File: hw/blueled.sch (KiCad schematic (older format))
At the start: 54 parts, among them J1 Barrel_Jack, J2 LED Strip, J3 ICSP, J4 Screw_Terminal_01x02, Q1 Q_PMOS_SDG, Q2 Q_PNP_EBC, SW2 PUSH, U1 ATmega328P-AU, U2 HC-05, U3 AMS1117-3.3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

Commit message: add(hw): resistor for ENA of DC/DC
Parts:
- added R12: 1k, Resistor_SMD:R_0805_2012Metric_Pad1.15x1.40mm_HandSolder, symbol Device:R
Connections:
- wire segments 197 -> 198
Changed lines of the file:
@@
 U 1 1 5FB2573B
 P 2200 1250
-F 0 "D4" H 2350 1350 50  0000 L CNN
-F 1 "D_Zener_ALT" H 2000 1450 50  0000 L CNN
+F 0 "D4" V 2200 1300 50  0000 L CNN
+F 1 "D_Zener_ALT" H 2000 1450 50  0001 L CNN
 F 2 "Diode_SMD:D_SOD-123" H 2200 1250 50  0001 C CNN
 F 3 "https://datasheet.lcsc.com/szlcsc/1912111437_PANJIT-International-MMSZ5240B_C268602.pdf" H 2200 1250 50  0001 C CNN
@@
 Wire Wire Line
 	2200 1000 2200 750
-Text Label 2800 2400 2    50   ~ 0
+Text Label 2800 2000 2    50   ~ 0
 PWR_PRT
 $Comp
@@
 Text Notes 750  5900 0    50   ~ 0
 Transistor is used to \nreset HC-05\nIt's need to switch to \nAT mode
+$Comp
+L Device:R R12
+U 1 1 5FD06E35
+P 2800 2250
+F 0 "R12" H 2870 2296 50  0000 L CNN
+F 1 "1k" H 2870 2205 50  0000 L CNN
+F 2 "Resistor_SMD:R_0805_2012Metric_Pad1.15x1.40mm_HandSolder" V 2730 2250 50  0001 C CNN
+F 3 "https://datasheet.lcsc.com/szlcsc/1810301711_KOA-Speer-Elec-RK73B2ATTD102J_C159911.pdf" H 2800 2250 50  0001 C CNN
+F 4 "lcsc.com" H 2800 2250 50  0001 C CNN "Distributor"
+F 5 "RK73B2ATTD102J" H 2800 2250 50  0001 C CNN "Manuf. Part"
+	1    2800 2250
+	1    0    0    -1
+$EndComp
+Wire Wire Line
+	2800 2000 2800 2100
 $EndSCHEMATC

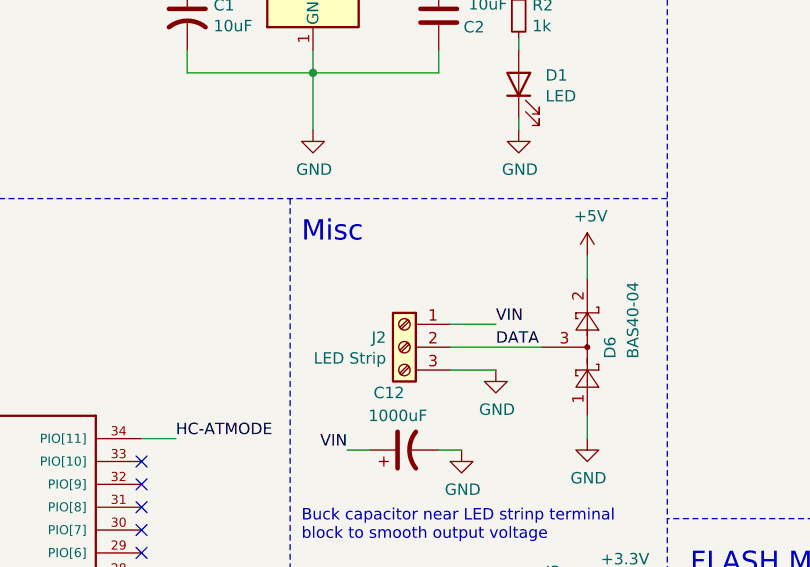
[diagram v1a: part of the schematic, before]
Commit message: add: better terminal block for led connection
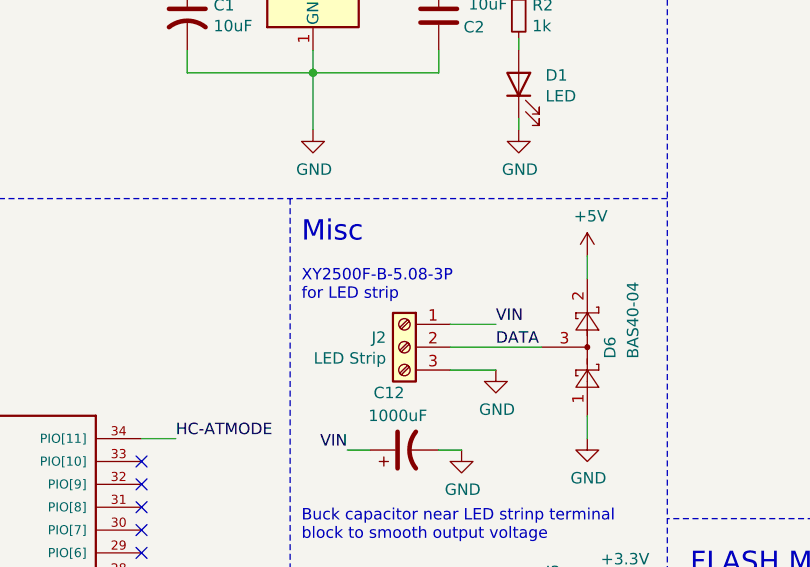
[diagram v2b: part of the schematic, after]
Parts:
- J2: footprint TerminalBlock:TerminalBlock_bornier-3_P5.08mm -> (none); Manuf. Part 1729131 -> XY2500R-D-5.08-3P
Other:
- note added: "XY2500F-B-5.08-3P \nfor LED strip\n"
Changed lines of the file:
@@
 F 0 "J2" H 5880 3842 50  0000 L CNN
 F 1 "LED Strip" H 5880 3751 50  0000 L CNN
-F 2 "TerminalBlock:TerminalBlock_bornier-3_P5.08mm" H 5800 3800 50  0001 C CNN
-F 3 "https://datasheet.lcsc.com/szlcsc/1811151432_Phoenix-Contact-1729131_C91154.pdf" H 5800 3800 50  0001 C CNN
+F 2 "" H 5800 3800 50  0001 C CNN
+F 3 "https://datasheet.lcsc.com/szlcsc/2004291906_Ningbo-Xinlaiya-Elec-XY2500R-D-5-08-3P_C505825.pdf" H 5800 3800 50  0001 C CNN
 F 4 "lcsc.com" H 5800 3800 50  0001 C CNN "Distributor"
-F 5 "1729131" H 5800 3800 50  0001 C CNN "Manuf. Part"
+F 5 "XY2500R-D-5.08-3P" H 5800 3800 50  0001 C CNN "Manuf. Part"
 	1    5800 3800
 	-1   0    0    -1
@@
 Wire Wire Line
 	2800 2000 2800 2100
+Text Notes 5350 3600 0    50   ~ 0
+XY2500F-B-5.08-3P \nfor LED strip\n
 $EndSCHEMATC

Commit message: fix: EN should be floating
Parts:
- removed R12: 1k, Resistor_SMD:R_0805_2012Metric_Pad1.15x1.40mm_HandSolder, symbol Device:R
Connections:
- wire segments 198 -> 195
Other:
- note added: "Float it to Enable"
- moved on the sheet: S1
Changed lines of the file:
@@
 Wire Wire Line
 	8850 3750 8950 3750
-Wire Wire Line
-	2900 2400 2800 2400
-NoConn ~ 2900 2900
-NoConn ~ 3300 2800
+NoConn ~ 2900 2650
+NoConn ~ 3300 2550
 $Comp
 L power:GND #PWR0110
@@
 	1    0    0    -1
 $EndComp
-NoConn ~ 2900 2700
+NoConn ~ 2900 2450
 $Comp
 L blueled-rescue:SWITCH-DPDT-PTH-GPI-152-3013-SparkFun-Switches S1
 U 1 1 5EB8E526
-P 3100 2700
-F 0 "S1" H 3100 2250 45  0000 C CNN
-F 1 "SWITCH-DPDT-PTH-GPI-152-3013" H 3100 3176 45  0001 C CNN
-F 2 "blueled:XKB7070-Z" H 3100 3150 20  0001 C CNN
-F 3 "https://datasheet.lcsc.com/szlcsc/2002271810_XKB-Enterprise-XKB7070-Z_C318863.pdf" H 3100 2700 50  0001 C CNN
-F 4 "SWCH-10554" H 3100 3081 60  0001 C CNN "Field4"
-F 5 "lcsc.com" H 3100 2700 50  0001 C CNN "Distributor"
-F 6 "XKB7070-Z" H 3100 2700 50  0001 C CNN "Manuf. Part"
-	1    3100 2700
+P 3100 2450
+F 0 "S1" H 3100 2000 45  0000 C CNN
+F 1 "SWITCH-DPDT-PTH-GPI-152-3013" H 3100 2926 45  0001 C CNN
+F 2 "blueled:XKB7070-Z" H 3100 2900 20  0001 C CNN
+F 3 "https://datasheet.lcsc.com/szlcsc/2002271810_XKB-Enterprise-XKB7070-Z_C318863.pdf" H 3100 2450 50  0001 C CNN
+F 4 "SWCH-10554" H 3100 2831 60  0001 C CNN "Field4"
+F 5 "lcsc.com" H 3100 2450 50  0001 C CNN "Distributor"
+F 6 "XKB7070-Z" H 3100 2450 50  0001 C CNN "Manuf. Part"
+	1    3100 2450
 	-1   0    0    1
 $EndComp
@@
 Wire Wire Line
 	3400 1200 3450 1200
-Text Label 3400 2500 0    50   ~ 0
+Text Label 3400 2250 0    50   ~ 0
 ENA
 Wire Wire Line
-	3300 2500 3400 2500
-Text Label 2200 750  0    50   ~ 0
-PWR_PRT
-Wire Wire Line
-	2200 1000 2200 750
-Text Label 2800 2000 2    50   ~ 0
-PWR_PRT
+	3300 2250 3400 2250
 $Comp
 L power:GND #PWR013
 U 1 1 6017A84C
-P 2800 2700
-F 0 "#PWR013" H 2800 2450 50  0001 C CNN
-F 1 "GND" H 2805 2527 50  0000 C CNN
-F 2 "" H 2800 2700 50  0001 C CNN
-F 3 "" H 2800 2700 50  0001 C CNN
-	1    2800 2700
-	1    0    0    -1
-$EndComp
-Wire Wire Line
-	2800 2700 2800 2600
-Wire Wire Line
-	2800 2600 2900 2600
+P 2800 2450
+F 0 "#PWR013" H 2800 2200 50  0001 C CNN
+F 1 "GND" H 2805 2277 50  0000 C CNN
+F 2 "" H 2800 2450 50  0001 C CNN
+F 3 "" H 2800 2450 50  0001 C CNN
+	1    2800 2450
+	1    0    0    -1
+$EndComp
+Wire Wire Line
+	2800 2450 2800 2350
+Wire Wire Line
+	2800 2350 2900 2350
 Wire Notes Line width 12
 	6950 3150 600  3150
@@
 Text Notes 750  5900 0    50   ~ 0
 Transistor is used to \nreset HC-05\nIt's need to switch to \nAT mode
-$Comp
-L Device:R R12
-U 1 1 5FD06E35
-P 2800 2250
-F 0 "R12" H 2870 2296 50  0000 L CNN
-F 1 "1k" H 2870 2205 50  0000 L CNN
-F 2 "Resistor_SMD:R_0805_2012Metric_Pad1.15x1.40mm_HandSolder" V 2730 2250 50  0001 C CNN
-F 3 "https://datasheet.lcsc.com/szlcsc/1810301711_KOA-Speer-Elec-RK73B2ATTD102J_C159911.pdf" H 2800 2250 50  0001 C CNN
-F 4 "lcsc.com" H 2800 2250 50  0001 C CNN "Distributor"
-F 5 "RK73B2ATTD102J" H 2800 2250 50  0001 C CNN "Manuf. Part"
-	1    2800 2250
-	1    0    0    -1
-$EndComp
-Wire Wire Line
-	2800 2000 2800 2100
 Text Notes 5350 3600 0    50   ~ 0
 XY2500F-B-5.08-3P \nfor LED strip\n
+Text Notes 3400 2350 0    50   ~ 0
+Float it to Enable
 $EndSCHEMATC

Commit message: add: power supply is based on LM25085
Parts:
- removed C11: 0.01uF, Capacitor_SMD:C_0805_2012Metric_Pad1.15x1.40mm_HandSolder, symbol Device:C
- removed C6, C7, C8: 4.7uF, Capacitor_SMD:C_0805_2012Metric_Pad1.15x1.40mm_HandSolder, symbol Device:C
- removed D4: D_Zener_ALT, Diode_SMD:D_SOD-123, symbol Device:D_Zener_ALT
- removed R8: 1k, Resistor_SMD:R_0805_2012Metric_Pad1.15x1.40mm_HandSolder, symbol Device:R
- removed U5: TPS5450, Package_SO:SOP-8_3.9x4.9mm_P1.27mm, symbol Regulator_Switching:TPS5450
- added C? (x2): 330uF, Capacitor_Tantalum_SMD:CP_EIA-3216-18_Kemet-A_Pad1.58x1.35mm_HandSolder, symbol Device:CP1
- added C?: 0.01uF, Capacitor_SMD:C_0805_2012Metric_Pad1.15x1.40mm_HandSolder, symbol Device:C
- added R? (x2): 1k, Resistor_SMD:R_0805_2012Metric_Pad1.15x1.40mm_HandSolder, symbol Device:R
- added U?: LM25085MM, Package_SO:MSOP-8_3x3mm_P0.65mm, symbol Regulator_Switching:LM25085MM
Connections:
- net labels added: SHUTDOWN
- net labels removed: ENA
- wire segments 195 -> 181
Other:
- note removed: "Float it to Enable"
- moved on the sheet: C1, C10, C2, C9, D1, D5, J1, J4, L1, Q1, R10, R2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

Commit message: add: missing comments (more to go)
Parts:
- added C?: 3300pF, symbol Device:C
- added R?: 66.5, symbol Device:R_Small
- C10: value 330uF -> 100uF; footprint Capacitor_Tantalum_SMD:CP_EIA-3216-18_Kemet-A_Pad1.58x1.35mm_HandSolder -> (none)
- C9: value 0.01uF -> 0.1uF; footprint Capacitor_SMD:C_0805_2012Metric_Pad1.15x1.40mm_HandSolder -> (none)
- C?: value 330uF -> 33uF; footprint Capacitor_Tantalum_SMD:CP_EIA-3216-18_Kemet-A_Pad1.58x1.35mm_HandSolder -> (none)
- C?: value 330uF -> 0.47uF; footprint Capacitor_Tantalum_SMD:CP_EIA-3216-18_Kemet-A_Pad1.58x1.35mm_HandSolder -> (none)
- C?: value 0.01uF -> 1000pF; footprint Capacitor_SMD:C_0805_2012Metric_Pad1.15x1.40mm_HandSolder -> (none)
- R10: value 3.16k -> 10k; footprint Resistor_SMD:R_0805_2012Metric_Pad1.15x1.40mm_HandSolder -> (none)
- R9: value 10k -> 3.4k; footprint Resistor_SMD:R_0805_2012Metric_Pad1.15x1.40mm_HandSolder -> (none)
- R?: value 1k -> 90.9
- R?: value 1k -> 2.1; footprint Resistor_SMD:R_0805_2012Metric_Pad1.15x1.40mm_HandSolder -> (none)
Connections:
- net +5V: now also C?.2; no longer C9.1
- net at D5.1 (K), L1.1, Q1.1 (S)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: now also R?.1
- new net: C9.1, C?.1, R?.2
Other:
- moved on the sheet: C10, C9, R10, R9

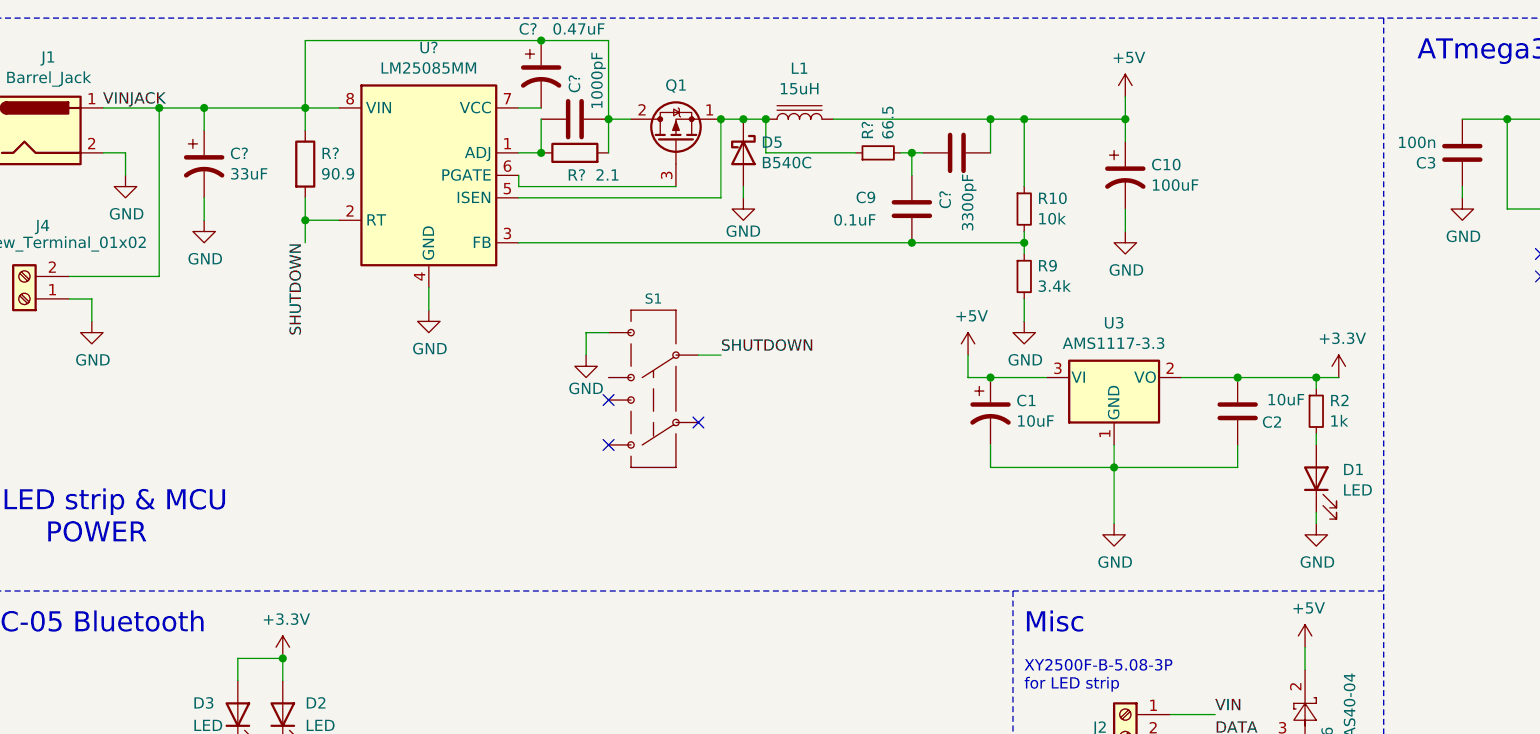
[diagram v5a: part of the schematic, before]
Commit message: fix(hw): more changes to power supply scheme
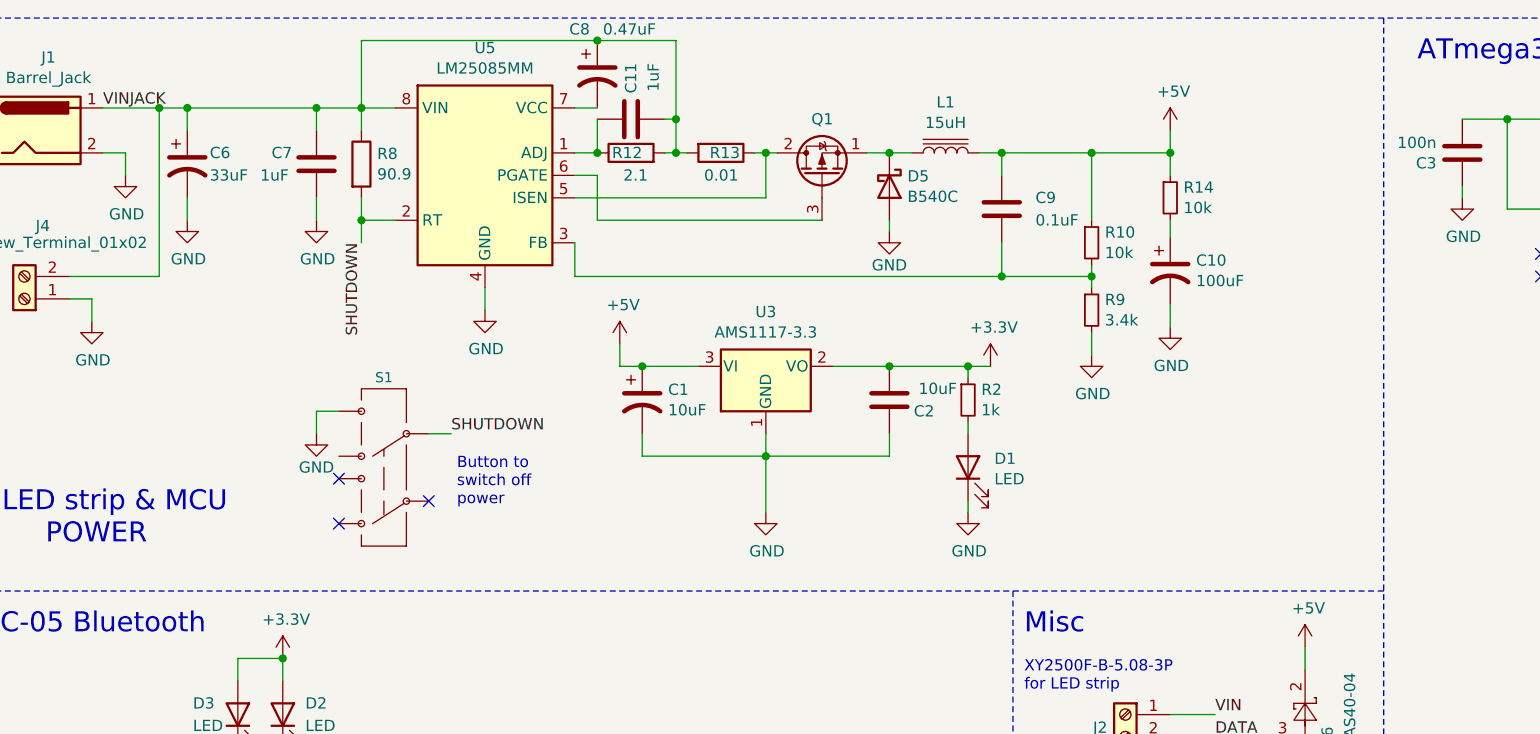
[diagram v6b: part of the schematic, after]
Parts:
- removed C?: 3300pF, symbol Device:C
- removed R?: 66.5, symbol Device:R_Small
- added C7: 1uF, symbol Device:C
- added R13: 0.01, symbol Device:R
- added R14: 10k, symbol Device:R_Small
- C11: renamed from C?; value 1000pF -> 1uF
- gave numbers to parts that had none: 5
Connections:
- net +5V: now also C9.1, R14.1; no longer C10.1
- net GND: now also C7.2
- net VINJACK: now also C7.1, R13.2; no longer Q1.2 (D)
- net at D5.1 (K), L1.1, Q1.1 (S): no longer U5.5 (ISEN)
- new net: Q1.2 (D), R13.1, U5.5 (ISEN)
- new net: C10.1, R14.2
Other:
- note added: "Button to \nswitch off \npower"
- moved on the sheet: C1, C10, C11, C2, C6, C8, C9, D1, D5, L1, Q1, R10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
